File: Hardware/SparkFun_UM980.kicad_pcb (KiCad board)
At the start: 2 copper layers, 50.8 x 50.8 mm, 141 parts, among them J1 USB_C_Receptacle, J2 Conn_01x12, J4 Qwiic_RA, J5 SMA_EdgeMount, J6 JST_Locking_4, J7 Qwiic_RA, J8 Conn_01x09, Q2 DMG2305UX, U1 TVS_DIODE_ARRAY, U2 AP2112K-3.3, U3 MCP6021T, U4 74LVC2G07, U5 UM980, U6 74LVC2G07, U8 CH340C

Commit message: Remove old files
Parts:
- added kibuzzard-64C3DF93: G***, kibuzzard-64C3DF93, B.Cu at (104.6, 129.5)
- moved G3 35.7 mm to (134.6, 113.1)
- moved G1 23.4 mm to (108.0, 163.8)
- moved kibuzzard-64C2EB16 3.60 mm to (148.6, 137.2)
- moved kibuzzard-64C2EB11 2.34 mm to (148.6, 135.9)
- moved kibuzzard-64C2E9FD 1.51 mm to (110.5, 116.0)
- moved kibuzzard-64C2E9F9 1.32 mm to (110.5, 113.9)
- moved kibuzzard-64C2E9F4 1.25 mm to (110.5, 111.8)
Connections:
- net Net-(U1-I/O3) renamed /D-
- net Net-(U1-I/O4) renamed /D+
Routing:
- net /D-: track 0.00 -> 15.1 mm, vias 0 -> 2
- net /D+: track 0.00 -> 13.2 mm
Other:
- board text added: "N. Seidle"

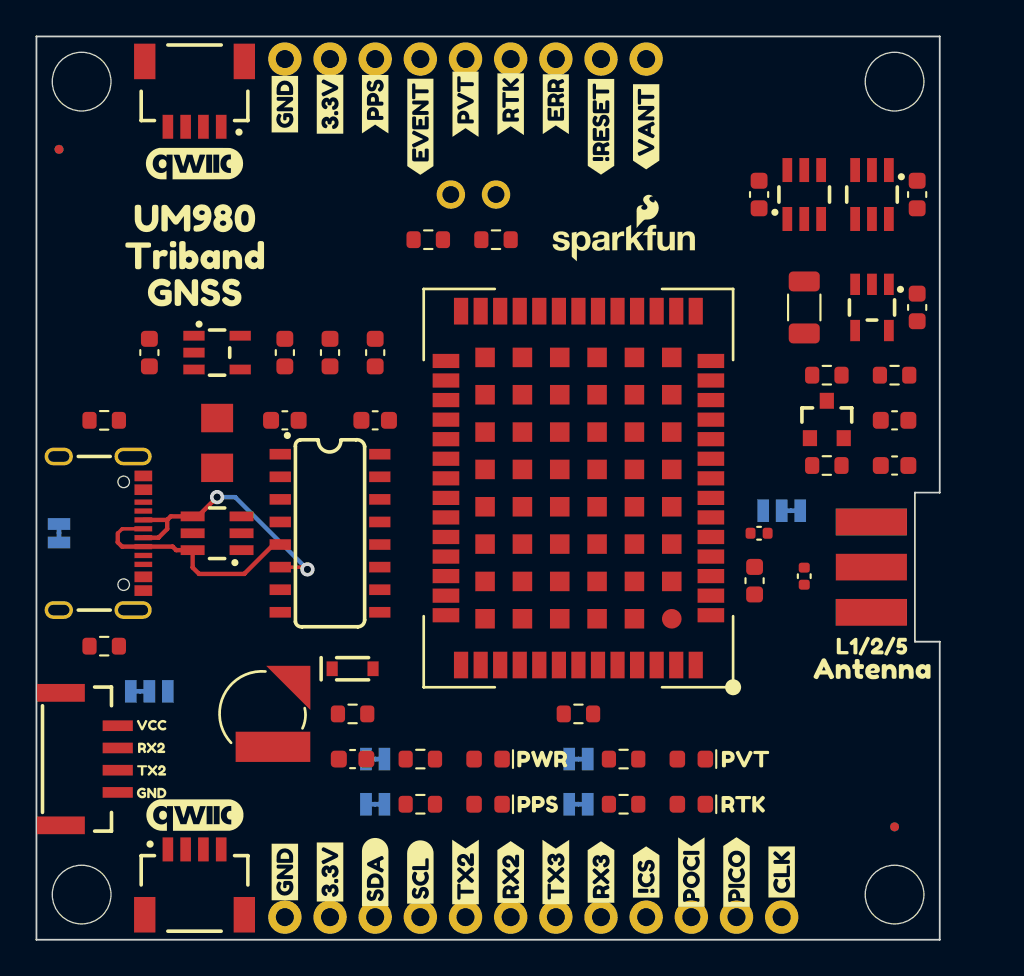
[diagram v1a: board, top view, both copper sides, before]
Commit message: Add silk. Remove linked logos in sch.
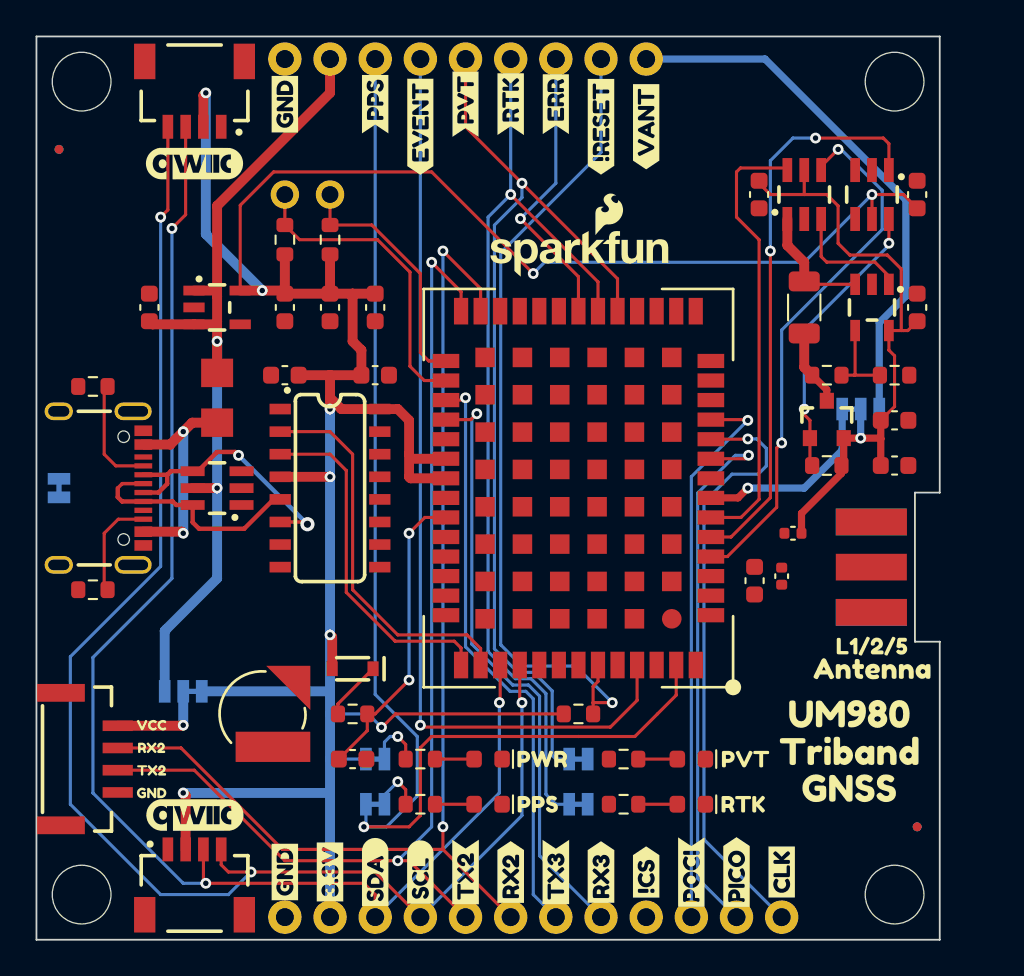
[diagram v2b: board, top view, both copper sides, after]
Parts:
- removed G3, G5: SparkFun_Logo, SparkFun-Aesthetic:SparkFun_Logo_8mm
- removed the kibuzzard-64C2E41E at (118.1, 105.4)
- removed the kibuzzard-64C2E455 at (118.1, 105.4)
- added G***: LOGO, SparkFun-Aesthetic:SparkFun_Logo_10mm, F.Cu at (132.1, 113.7)
- added G***: LOGO, SparkFun-Aesthetic:SparkFun_Logo_10mm, B.Cu at (127.0, 120.7)
- added kibuzzard-64C41486: G***, kibuzzard-64C41486, B.Cu at (148.0, 120.8)
- added kibuzzard-64C414AC: G***, kibuzzard-64C414AC, B.Cu at (150.5, 122.6)
- added kibuzzard-64C414C1: G***, kibuzzard-64C414C1, B.Cu at (145.4, 122.6)
- moved kibuzzard-64C2E9F9 46.2 mm to (147.3, 141.8)
- moved kibuzzard-64C2E9FD 46.2 mm to (147.3, 143.9)
- moved kibuzzard-64C2E9F4 46.2 mm to (147.3, 139.7)
- moved U7 33.0 mm to (165.1, 101.6)
- moved kibuzzard-64C2EAF0 10.4 mm to (120.0, 110.5), turned to -90 degrees
- moved TP2 9.34 mm to (115.6, 110.5)
- moved R14 9.33 mm to (118.1, 113.0), turned to 90 degrees
- moved TP1 9.33 mm to (118.1, 110.5)
- moved kibuzzard-64C2EADB 8.25 mm to (113.7, 110.5), turned to -90 degrees
- moved R13 8.07 mm to (115.6, 113.0), turned to 90 degrees
- moved JP1 7.24 mm to (148.0, 122.6)
- moved kibuzzard-64C2E9F4 5.08 mm to (127.0, 124.5)
- moved kibuzzard-64C2E9F9 5.08 mm to (127.0, 127.0)
- moved kibuzzard-64C2E9FD 5.08 mm to (127.0, 129.5)
- moved R1 3.24 mm to (104.8, 132.7)
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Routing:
- net +3.3V: track 0.00 -> 165.9 mm, vias 0 -> 9
- net SCL: track 0.00 -> 83.0 mm, vias 0 -> 3
- net SDA: track 0.00 -> 78.2 mm, vias 0 -> 3
- net PPS: track 0.00 -> 72.0 mm, vias 0 -> 1
- net RXD2: track 0.00 -> 64.0 mm, vias 0 -> 2
- net TXD2: track 0.00 -> 60.9 mm, vias 0 -> 2
- net RTK_STAT: track 0.00 -> 53.9 mm, vias 0 -> 1
- net PVT_STAT: track 0.00 -> 53.4 mm, vias 0 -> 1
- net EVENT: track 0.00 -> 52.3 mm, vias 0 -> 1
- net +5V: track 0.00 -> 47.5 mm, vias 0 -> 2
- net ~{RESET}: track 0.00 -> 46.8 mm, vias 0 -> 1
- net ANT_BIAS: track 0.00 -> 36.3 mm, vias 0 -> 1
- net SPI_CLK: track 0.00 -> 33.8 mm, vias 0 -> 1
- net RXD3: track 0.00 -> 33.8 mm, vias 0 -> 1
- net TXD3: track 0.00 -> 33.0 mm, vias 0 -> 1
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
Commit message: Update design with PROD_IDs
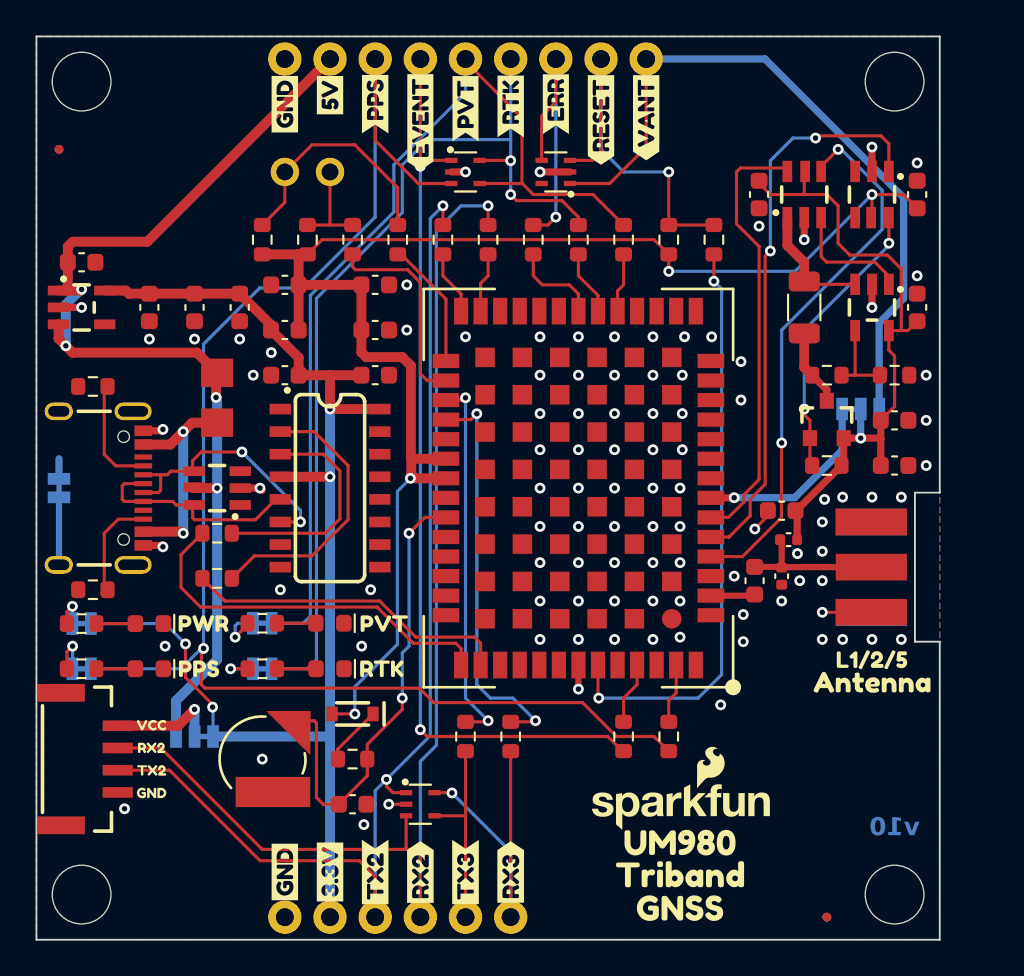
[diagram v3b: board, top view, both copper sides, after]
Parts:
- removed G2, G4: LOGO, SparkFun-Aesthetic:qwiic_5.5mm
- removed J2: Conn_01x12, SparkFun-Connector:1X12
- removed J4, J7: Qwiic_RA, SparkFun-Connector:JST04_1MM_RA
- removed kibuzzard-64C2D98D: G***, kibuzzard-64C2D98D
- removed kibuzzard-64C2D999: G***, kibuzzard-64C2D999
- removed kibuzzard-64C2D9AB: G***, kibuzzard-64C2D9AB
- removed kibuzzard-64C2E3AA: G***, kibuzzard-64C2E3AA
- removed kibuzzard-64C2E3B2: G***, kibuzzard-64C2E3B2
- removed kibuzzard-64C2E47D: G***, kibuzzard-64C2E47D
- removed kibuzzard-64C2E486: G***, kibuzzard-64C2E486
- removed kibuzzard-64C2E4C6: G***, kibuzzard-64C2E4C6
- removed kibuzzard-64C2E4D6: G***, kibuzzard-64C2E4D6
- removed kibuzzard-64C2E4E9: G***, kibuzzard-64C2E4E9
- removed kibuzzard-64C2E4EF: G***, kibuzzard-64C2E4EF
- removed kibuzzard-64C2E4F9: G***, kibuzzard-64C2E4F9
- removed kibuzzard-64C2E581: G***, kibuzzard-64C2E581
- removed kibuzzard-64C2E706: G***, kibuzzard-64C2E706
- removed kibuzzard-64C2E713: G***, kibuzzard-64C2E713
- removed the kibuzzard-64C2E9F4 at (147.3, 139.7)
- removed the kibuzzard-64C2E9F9 at (147.3, 141.8)
- removed the kibuzzard-64C2E9FD at (147.3, 143.9)
- removed kibuzzard-64C2EA8F: G***, kibuzzard-64C2EA8F
- added C14: 0.1uF, SparkFun-Capacitor:C_0603_1608Metric, F.Cu at (143.5, 128.3)
- added C15: 22uF, SparkFun-Capacitor:C_0603_1608Metric, F.Cu at (120.7, 118.1)
- added C16: 0.1uF, SparkFun-Capacitor:C_0603_1608Metric, F.Cu at (115.6, 115.6)
- added C17: 22uF, SparkFun-Capacitor:C_0603_1608Metric, F.Cu at (120.7, 115.6)
- added D10: PESD3V3L4UG, SparkFun-Semiconductor-Standard:SOT-353, F.Cu at (125.7, 109.2)
- added D11: PESD3V3L4UG, SparkFun-Semiconductor-Standard:SOT-353, F.Cu at (130.8, 109.2)
- added D9: PESD3V3L4UG, SparkFun-Semiconductor-Standard:SOT-353, F.Cu at (123.2, 144.8)
- added J3: Conn_01x06, SparkFun-Connector:1X06, F.Cu at (128.3, 151.1)
- added L2: 30Ω, SparkFun-Capacitor:C_0603_1608Metric, F.Cu at (115.6, 118.1)
- added R15: 33, SparkFun-Resistor:R_0603_1608Metric, F.Cu at (111.8, 129.5)
- added R16: 33, SparkFun-Resistor:R_0603_1608Metric, F.Cu at (111.8, 132.1)
- added R17: 33, SparkFun-Resistor:R_0603_1608Metric, F.Cu at (124.5, 113.0)
- added R18: 33, SparkFun-Resistor:R_0603_1608Metric, F.Cu at (127.0, 113.0)
- added R19: 33, SparkFun-Resistor:R_0603_1608Metric, F.Cu at (125.7, 141.0)
- added R20: 33, SparkFun-Resistor:R_0603_1608Metric, F.Cu at (128.3, 141.0)
- added R27: 33, SparkFun-Resistor:R_0603_1608Metric, F.Cu at (129.5, 113.0)
- added R28: 33, SparkFun-Resistor:R_0603_1608Metric, F.Cu at (132.1, 113.0)
- added R29: 33, SparkFun-Resistor:R_0603_1608Metric, F.Cu at (134.6, 113.0)
- added R30: 33, SparkFun-Resistor:R_0603_1608Metric, F.Cu at (137.2, 141.0)
- added R31: 33, SparkFun-Resistor:R_0603_1608Metric, F.Cu at (134.6, 141.0)
- added R32: 33, SparkFun-Resistor:R_0603_1608Metric, F.Cu at (121.9, 113.0)
- added R33: 33, SparkFun-Resistor:R_0603_1608Metric, F.Cu at (119.4, 113.0)
- added R34: 33, SparkFun-Resistor:R_0603_1608Metric, F.Cu at (139.7, 113.0)
- added kibuzzard-64C982F1: G***, kibuzzard-64C982F1, B.Cu at (133.3, 106.3)
- added kibuzzard-64C982F7: G***, kibuzzard-64C982F7, F.Cu at (133.3, 106.3)
- added kibuzzard-64C9834C: G***, kibuzzard-64C9834C, F.Cu at (118.1, 104.9)
- added kibuzzard-64C98351: G***, kibuzzard-64C98351, B.Cu at (118.1, 104.9)
- added kibuzzard-64CB1646: G***, kibuzzard-64CB1646, B.Cu at (107.4, 134.6)
- added kibuzzard-64CB1658: G***, kibuzzard-64CB1658, B.Cu at (107.2, 137.2)
- added kibuzzard-64D2969C: G***, kibuzzard-64D2969C, F.Cu at (137.8, 146.9)
- added kibuzzard-64D296A7: G***, kibuzzard-64D296A7, F.Cu at (137.8, 148.7)
- added kibuzzard-64D296AE: G***, kibuzzard-64D296AE, F.Cu at (137.8, 150.6)
- moved G*** 31.6 mm to (137.8, 144.8)
- moved R12 27.1 mm to (137.2, 113.0), turned to 90 degrees
- moved D3 21.7 mm to (118.1, 134.6)
- moved R6 21.7 mm to (114.3, 134.6)
- moved D2 21.7 mm to (118.1, 137.2)
- moved R3 21.7 mm to (114.3, 137.2)
- moved kibuzzard-64C2E6C9 21.7 mm to (121.2, 134.6)
- moved kibuzzard-64C2E6D6 21.7 mm to (121.0, 137.2)
- moved kibuzzard-64C2E6BD 20.5 mm to (110.7, 137.2)
- moved D1 20.5 mm to (108.0, 134.6)
- moved D4 20.5 mm to (108.0, 137.2)
- moved R4 20.5 mm to (104.1, 134.6)
- moved R5 20.5 mm to (104.1, 137.2)
- moved kibuzzard-64C2E6A3 20.5 mm to (111.0, 134.6)
- moved JP4 19.4 mm to (114.3, 134.6), turned to 0 degrees
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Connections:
- C11 pad 1: +3.3V -> +3.3V_A
- D5 pad A: +3.3V -> +3.3V_A
- J1 pad A8: (no net) -> unconnected-(J1-NC-PadA8)
- J1 pad B8: (no net) -> unconnected-(J1-NC-PadB8)
- J6 pad NC1: (no net) -> unconnected-(J6-NC-PadNC1)
- J6 pad NC2: (no net) -> unconnected-(J6-NC-PadNC2)
- L1 pad 1: Net-(D6-A2) -> ANT_BIAS
- L1 pad 2: ANT_BIAS -> Net-(D6-A2)
- R12 pad 1: +3.3V -> +3.3V_A
- R13 pad 1: +3.3V -> +3.3V_A
- R13 pad 2: Net-(U5-BIF_29) -> Net-(R13-Pad2)
- R14 pad 1: +3.3V -> +3.3V_A
- R14 pad 2: Net-(U5-BIF_28) -> Net-(R14-Pad2)
- TP1 pad 1: Net-(U5-BIF_28) -> Net-(R13-Pad2)
- TP2 pad 1: Net-(U5-BIF_29) -> Net-(R14-Pad2)
- U5 pad 10: SPI_CLK -> unconnected-(U5-SPI_CLK-Pad10)
- U5 pad 11: SPI_POCI -> unconnected-(U5-SPI_POCI-Pad11)
- U5 pad 13: (no net) -> unconnected-(U5-NC-Pad13)
- U5 pad 15: (no net) -> unconnected-(U5-NC-Pad15)
- U5 pad 16: (no net) -> unconnected-(U5-NC-Pad16)
- U5 pad 17: (no net) -> unconnected-(U5-NC-Pad17)
- U5 pad 18: (no net) -> unconnected-(U5-NC-Pad18)
- U5 pad 19: PVT_STAT -> Net-(U5-PVT_STAT)
- U5 pad 20: RTK_STAT -> Net-(U5-RTK_STAT)
- U5 pad 21: ERR_STAT -> Net-(U5-ERR_STAT)
- U5 pad 22: (no net) -> unconnected-(U5-NC-Pad22)
- U5 pad 23: (no net) -> unconnected-(U5-NC-Pad23)
- U5 pad 24: (no net) -> unconnected-(U5-NC-Pad24)
- U5 pad 25: (no net) -> unconnected-(U5-NC-Pad25)
- U5 pad 26: RXD2 -> Net-(U5-RXD2)
- U5 pad 27: TXD2 -> Net-(U5-TXD2)
- U5 pad 30: TXD3 -> Net-(U5-TXD3)
- U5 pad 31: RXD3 -> Net-(U5-RXD3)
- U5 pad 33: +3.3V -> +3.3V_A
- U5 pad 34: +3.3V -> +3.3V_A
- U5 pad 35: (no net) -> unconnected-(U5-NC-Pad35)
- U5 pad 38: (no net) -> unconnected-(U5-NC-Pad38)
- U5 pad 39: (no net) -> unconnected-(U5-NC-Pad39)
- U5 pad 40: (no net) -> unconnected-(U5-NC-Pad40)
- U5 pad 42: TXD1 -> Net-(U5-TXD1)
- U5 pad 43: RXD1 -> Net-(U5-RXD1)
- U5 pad 44: SDA -> unconnected-(U5-SDA-Pad44)
- U5 pad 45: SCL -> unconnected-(U5-SCL-Pad45)
- U5 pad 46: (no net) -> unconnected-(U5-NC-Pad46)
- U5 pad 47: (no net) -> unconnected-(U5-NC-Pad47)
- U5 pad 49: ~{RESET} -> Net-(U5-~{RESET})
- U5 pad 50: (no net) -> unconnected-(U5-NC-Pad50)
- U5 pad 51: EVENT -> Net-(U5-EVENT)
- U5 pad 52: (no net) -> unconnected-(U5-NC-Pad52)
- U5 pad 53: PPS -> Net-(U5-PPS)
- U5 pad 54: (no net) -> unconnected-(U5-NC-Pad54)
- U5 pad 8: SPI_~{CS} -> unconnected-(U5-SPI_~{CS}-Pad8)
- U5 pad 9: SPI_PICO -> unconnected-(U5-SPI_PICO-Pad9)
- U6 pad 3: (no net) -> unconnected-(U6-Pad3)
- U6 pad 4: (no net) -> unconnected-(U6-Pad4)
- U6 pad 5: +3.3V -> +3.3V_A
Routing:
- net +3.3V: track 165.9 -> 71.5 mm, vias 9 -> 4
- net SCL: track 83.0 -> 0.00 mm, vias 3 -> 0
- net +3.3V_A: track 0.00 -> 82.6 mm, vias 0 -> 4
- net SDA: track 78.2 -> 0.00 mm, vias 3 -> 0
- net SPI_CLK: track 33.8 -> 0.00 mm, vias 1 -> 0
- net Net-(U5-~{RESET}): track 0.00 -> 33.1 mm, vias 0 -> 2
- net SPI_POCI: track 31.3 -> 0.00 mm, vias 1 -> 0
- net SPI_PICO: track 30.7 -> 0.00 mm, vias 1 -> 0
- net ~{RESET}: track 46.8 -> 22.1 mm
- net Net-(U5-RXD3): track 0.00 -> 22.7 mm, vias 0 -> 2
- net TXD3: track 33.0 -> 11.1 mm, vias 1 -> 0
- net Net-(U5-TXD1): track 0.00 -> 21.7 mm
- net Net-(U5-TXD3): track 0.00 -> 21.1 mm, vias 0 -> 2
- net GND: track 0.00 -> 18.8 mm, vias 0 -> 100
- net Net-(U5-RXD1): track 0.00 -> 18.4 mm
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- added copper zone on B.Cu, net GND
- added copper zone on F.Cu, net GND
- added copper zone on In1.Cu, net GND
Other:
- copper layers 2 -> 4
- board text added: "Route Out"
- board text added: "v10"
